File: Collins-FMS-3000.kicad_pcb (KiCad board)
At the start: 2 copper layers, 145 x 160 mm, 196 parts, among them J1 USB_B_Mini, J2 AVR-ISP-6, J3 Conn_01x04, SW1 SW_Push_LED, SW10 SW_Push_LED, SW11 SW_Push_LED, SW12 SW_Push_LED, SW13 SW_Push_LED, SW14 SW_Push_LED, SW15 SW_Push_LED, SW16 SW_Push_LED, SW17 SW_Push_LED, SW18 SW_Push_LED, SW19 SW_Push_LED, SW2 SW_Push_LED, SW20 SW_Push_LED, SW21 SW_Push_LED, SW22 SW_Push_LED, SW23 SW_Push_LED, SW24 SW_Push_LED, SW25 SW_Push_LED, SW26 SW_Push_LED, SW27 SW_Push_LED, SW28 SW_Push_LED, SW29 SW_Push_LED, SW3 SW_Push_LED, SW30 SW_Push_LED, SW31 SW_Push_LED, SW32 SW_Push_LED, SW33 SW_Push_LED, SW34 SW_Push_LED, SW35 SW_Push_LED, SW36 SW_Push_LED, SW37 SW_Push_LED, SW38 SW_Push_LED, SW39 SW_Push_LED, SW4 SW_Push_LED, SW40 SW_Push_LED, SW41 SW_Push_LED, SW42 SW_Push_LED, SW43 SW_Push_LED, SW44 SW_Push_LED, SW45 SW_Push_LED, SW46 SW_Push_LED, SW47 SW_Push_LED, SW48 SW_Push_LED, SW49 SW_Push_LED, SW5 SW_Push_LED, SW50 SW_Push_LED, SW51 SW_Push_LED, SW52 SW_Push_LED, SW53 SW_Push_LED, SW54 SW_Push_LED, SW55 SW_Push_LED, SW56 SW_Push_LED, SW57 SW_Push_LED, SW58 SW_Push_LED, SW59 SW_Push_LED, SW6 SW_Push_LED, SW60 SW_Push_LED, SW61 SW_Push_LED, SW62 SW_Push_LED, SW63 SW_Push_LED, SW64 SW_Push_LED, SW65 SW_Push_LED, SW66 SW_Push_LED, SW67 SW_Push_LED, SW68 SW_Push_LED, SW69 SW_Push_LED, SW7 SW_Push_LED, SW70 SW_Push, SW8 SW_Push_LED, SW9 SW_Push_LED, U1 ATmega32U4-MU, U2 MCP23017_SO, U3 MCP23017_SO, U4 IS31FL3733B, Y1 16MHz

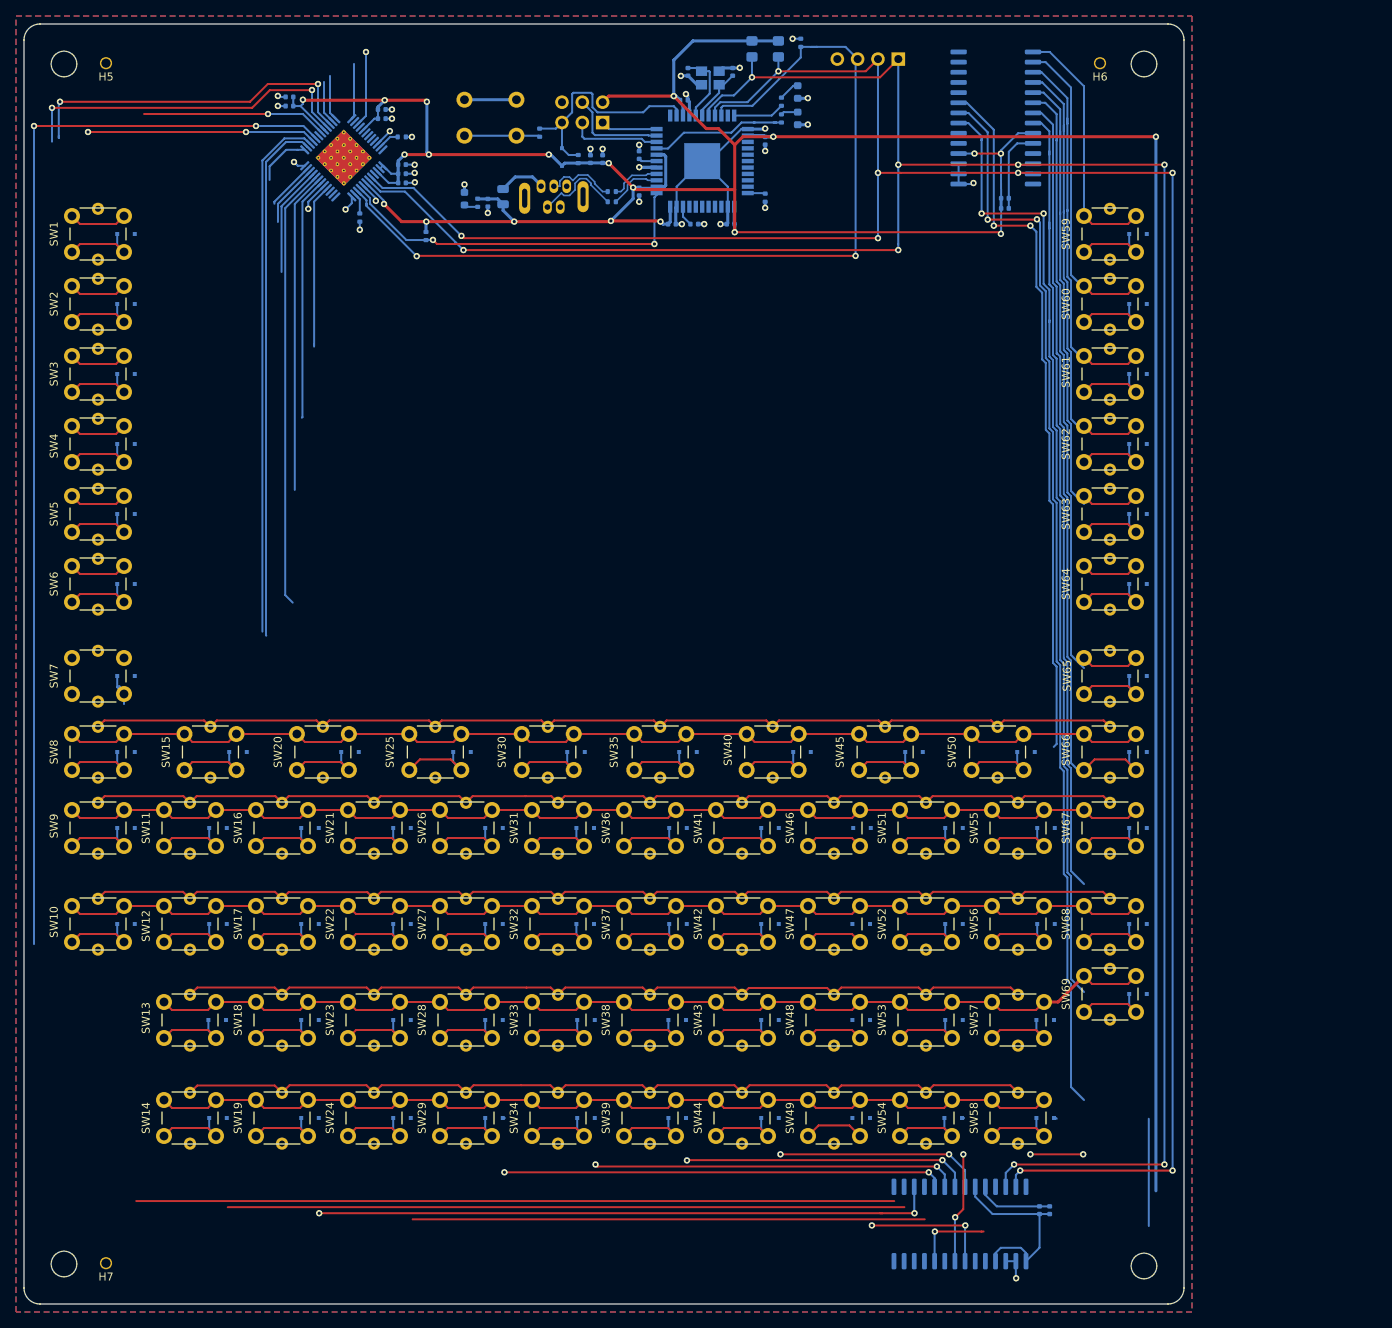
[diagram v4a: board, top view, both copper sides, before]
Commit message: Remove diodes, update interrupt connections
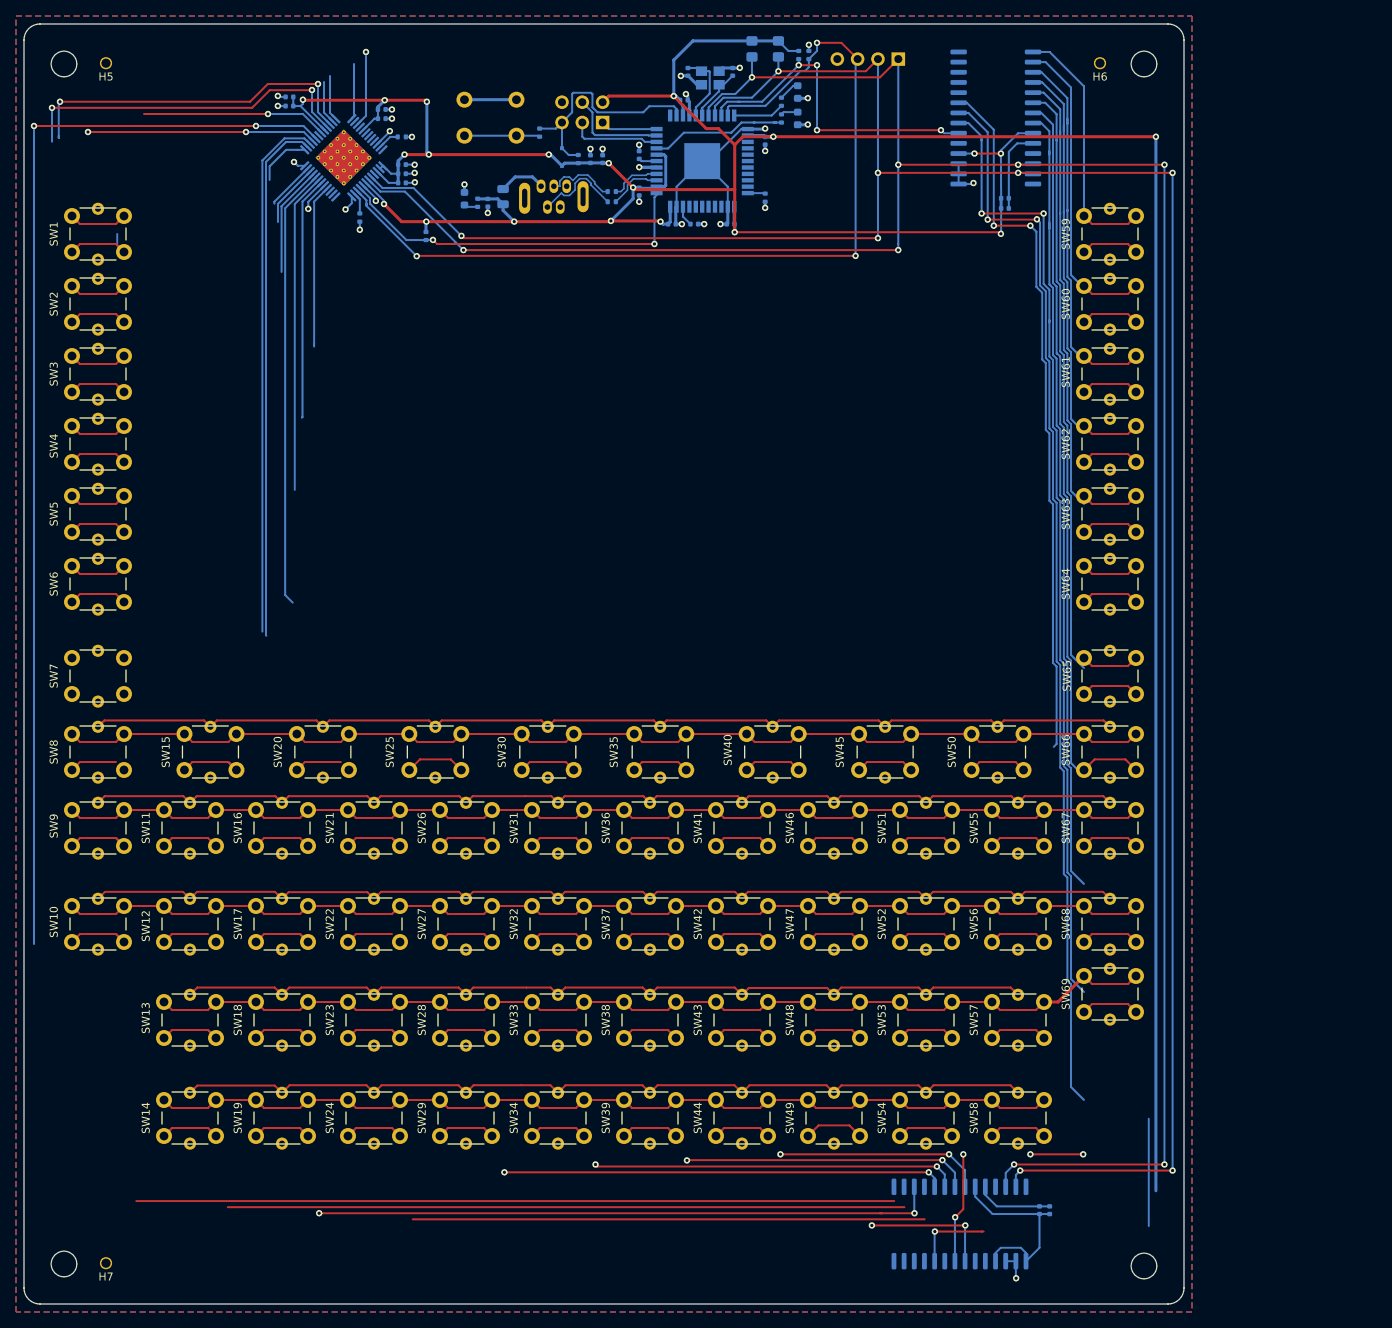
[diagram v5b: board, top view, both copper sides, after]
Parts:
- removed D1, D10, D11, D12, D13, D14, D15, D16, D17, D18, D19, D2, D20, D21, D22, D23, D24, D25, D26, D27, D28, D29, D3, D30, D31, D32, D33, D34, D35, D36, D37, D38, D39, D4, D40, D41, D42, D43, D44, D45, D46, D47, D48, D49, D5, D50, D51, D52, D53, D54, D55, D56, D57, D58, D59, D6, D60, D61, D62, D63, D64, D65, D66, D67, D68, D69, D7, D8, D9: D_Small, Diode_SMD:D_SOD-323F
- added R5: 100k, Resistor_SMD:R_0402_1005Metric, B.Cu at (116.8, 23.9)
- moved R3 1.83 mm to (118.1, 23.9)
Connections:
- net INTB renamed LED_INTB
- SW1 pad 2: Net-(D1-Pad2) -> /ButtonMatrix/COL0
- SW10 pad 2: Net-(D10-Pad2) -> /ButtonMatrix/COL0
- SW11 pad 2: Net-(D11-Pad2) -> /ButtonMatrix/COL1
- SW12 pad 2: Net-(D12-Pad2) -> /ButtonMatrix/COL1
- SW13 pad 2: Net-(D13-Pad2) -> /ButtonMatrix/COL1
- SW14 pad 2: Net-(D14-Pad2) -> /ButtonMatrix/COL1
- SW15 pad 2: Net-(D15-Pad2) -> /ButtonMatrix/COL2
- SW16 pad 2: Net-(D16-Pad2) -> /ButtonMatrix/COL2
- SW17 pad 2: Net-(D17-Pad2) -> /ButtonMatrix/COL2
- SW18 pad 2: Net-(D18-Pad2) -> /ButtonMatrix/COL2
- SW19 pad 2: Net-(D19-Pad2) -> /ButtonMatrix/COL2
- SW2 pad 2: Net-(D2-Pad2) -> /ButtonMatrix/COL0
- SW20 pad 2: Net-(D20-Pad2) -> /ButtonMatrix/COL3
- SW21 pad 2: Net-(D21-Pad2) -> /ButtonMatrix/COL3
- SW22 pad 2: Net-(D22-Pad2) -> /ButtonMatrix/COL3
- SW23 pad 2: Net-(D23-Pad2) -> /ButtonMatrix/COL3
- SW24 pad 2: Net-(D24-Pad2) -> /ButtonMatrix/COL3
- SW25 pad 2: Net-(D25-Pad2) -> /ButtonMatrix/COL4
- SW26 pad 2: Net-(D26-Pad2) -> /ButtonMatrix/COL4
- SW27 pad 2: Net-(D27-Pad2) -> /ButtonMatrix/COL4
- SW28 pad 2: Net-(D28-Pad2) -> /ButtonMatrix/COL4
- SW29 pad 2: Net-(D29-Pad2) -> /ButtonMatrix/COL4
- SW3 pad 2: Net-(D3-Pad2) -> /ButtonMatrix/COL0
- SW30 pad 2: Net-(D30-Pad2) -> /ButtonMatrix/COL5
- SW31 pad 2: Net-(D31-Pad2) -> /ButtonMatrix/COL5
- SW32 pad 2: Net-(D32-Pad2) -> /ButtonMatrix/COL5
- SW33 pad 2: Net-(D33-Pad2) -> /ButtonMatrix/COL5
- SW34 pad 2: Net-(D34-Pad2) -> /ButtonMatrix/COL5
- SW35 pad 2: Net-(D35-Pad2) -> /ButtonMatrix/COL6
- SW36 pad 2: Net-(D36-Pad2) -> /ButtonMatrix/COL6
- SW37 pad 2: Net-(D37-Pad2) -> /ButtonMatrix/COL6
- SW38 pad 2: Net-(D38-Pad2) -> /ButtonMatrix/COL6
- SW39 pad 2: Net-(D39-Pad2) -> /ButtonMatrix/COL6
- SW4 pad 2: Net-(D4-Pad2) -> /ButtonMatrix/COL0
- SW40 pad 2: Net-(D40-Pad2) -> /ButtonMatrix/COL7
- SW41 pad 2: Net-(D41-Pad2) -> /ButtonMatrix/COL7
- SW42 pad 2: Net-(D42-Pad2) -> /ButtonMatrix/COL7
- SW43 pad 2: Net-(D43-Pad2) -> /ButtonMatrix/COL7
- SW44 pad 2: Net-(D44-Pad2) -> /ButtonMatrix/COL7
- SW45 pad 2: Net-(D45-Pad2) -> /ButtonMatrix/COL8
- SW46 pad 2: Net-(D46-Pad2) -> /ButtonMatrix/COL8
- SW47 pad 2: Net-(D47-Pad2) -> /ButtonMatrix/COL8
- SW48 pad 2: Net-(D48-Pad2) -> /ButtonMatrix/COL8
- SW49 pad 2: Net-(D49-Pad2) -> /ButtonMatrix/COL8
- SW5 pad 2: Net-(D5-Pad2) -> /ButtonMatrix/COL0
- SW50 pad 2: Net-(D50-Pad2) -> /ButtonMatrix/COL9
- SW51 pad 2: Net-(D51-Pad2) -> /ButtonMatrix/COL9
- SW52 pad 2: Net-(D52-Pad2) -> /ButtonMatrix/COL9
- SW53 pad 2: Net-(D53-Pad2) -> /ButtonMatrix/COL9
- SW54 pad 2: Net-(D54-Pad2) -> /ButtonMatrix/COL9
- SW55 pad 2: Net-(D55-Pad2) -> /ButtonMatrix/COL10
- SW56 pad 2: Net-(D56-Pad2) -> /ButtonMatrix/COL10
- SW57 pad 2: Net-(D57-Pad2) -> /ButtonMatrix/COL10
- SW58 pad 2: Net-(D58-Pad2) -> /ButtonMatrix/COL10
- SW59 pad 2: Net-(D59-Pad2) -> /ButtonMatrix/COL11
- SW6 pad 2: Net-(D6-Pad2) -> /ButtonMatrix/COL0
- SW60 pad 2: Net-(D60-Pad2) -> /ButtonMatrix/COL11
- SW61 pad 2: Net-(D61-Pad2) -> /ButtonMatrix/COL11
- SW62 pad 2: Net-(D62-Pad2) -> /ButtonMatrix/COL11
- SW63 pad 2: Net-(D63-Pad2) -> /ButtonMatrix/COL11
- SW64 pad 2: Net-(D64-Pad2) -> /ButtonMatrix/COL11
- SW65 pad 2: Net-(D65-Pad2) -> /ButtonMatrix/COL11
- SW66 pad 2: Net-(D66-Pad2) -> /ButtonMatrix/COL11
- SW67 pad 2: Net-(D67-Pad2) -> /ButtonMatrix/COL11
- SW68 pad 2: Net-(D68-Pad2) -> /ButtonMatrix/COL11
- SW69 pad 2: Net-(D69-Pad2) -> /ButtonMatrix/COL11
- SW7 pad 2: Net-(D7-Pad2) -> /ButtonMatrix/COL0
- SW8 pad 2: Net-(D8-Pad2) -> /ButtonMatrix/COL0
- SW9 pad 2: Net-(D9-Pad2) -> /ButtonMatrix/COL0
- U1 pad 20: SDB -> ROW_INTA
- U1 pad 21: Net-(U1-Pad21) -> SDB
- U2 pad 20: Net-(U2-Pad20) -> ROW_INTA
- U4 pad 43: +5V -> GND
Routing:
- net /ButtonMatrix/COL11: track 23.2 -> 97.5 mm
- net /ButtonMatrix/COL0: track 94.7 -> 164.6 mm
- net ROW_INTA: track 0.00 -> 42.1 mm, vias 0 -> 4
- net /ButtonMatrix/COL2: track 78.3 -> 118.6 mm
- net /ButtonMatrix/COL4: track 55.4 -> 94.6 mm
- net /ButtonMatrix/COL8: track 16.2 -> 53.1 mm
- net /ButtonMatrix/COL5: track 45.9 -> 82.6 mm
- net /ButtonMatrix/COL7: track 26.0 -> 62.7 mm
- net /ButtonMatrix/COL6: track 36.1 -> 72.8 mm
- net /ButtonMatrix/COL9: track 13.9 -> 50.4 mm
- net /ButtonMatrix/COL3: track 64.0 -> 100.2 mm
- net /ButtonMatrix/COL1: track 84.6 -> 113.8 mm
- net /ButtonMatrix/COL10: track 0.14 -> 29.3 mm
- net Net-(D69-Pad2): track 10.9 -> 0.00 mm
- net Net-(D25-Pad2): track 10.3 -> 0.00 mm
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
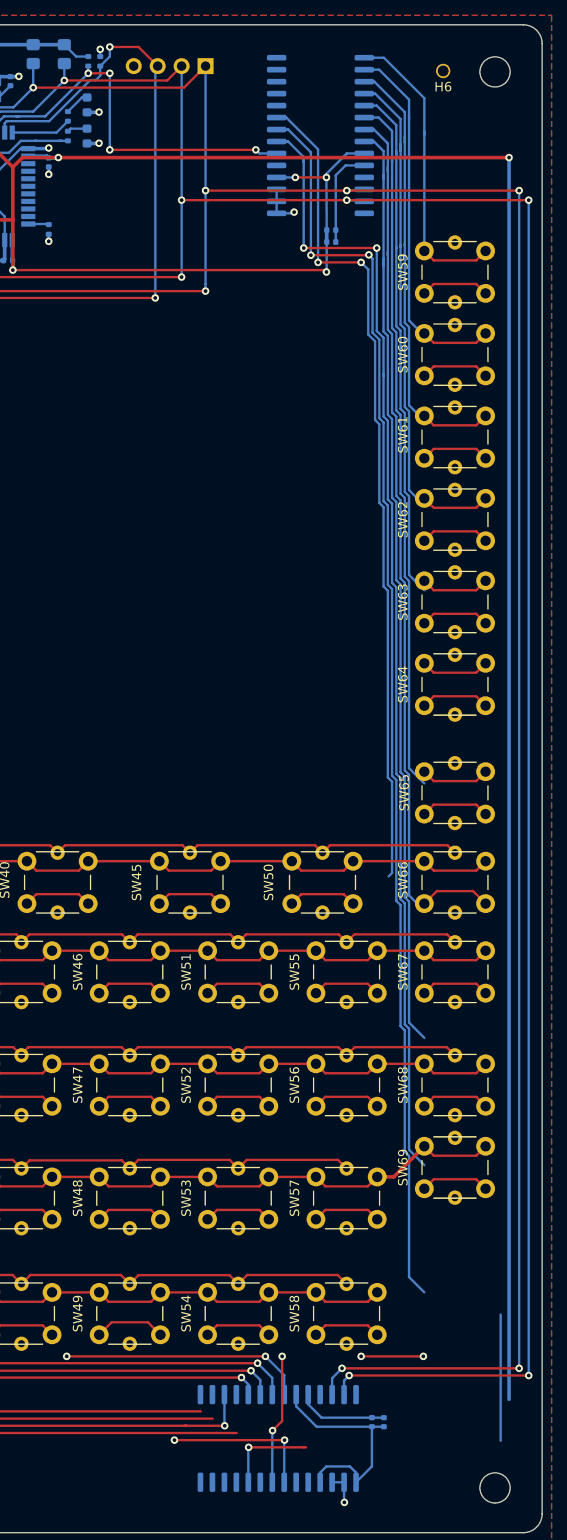
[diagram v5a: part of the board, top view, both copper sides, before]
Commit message: Connect unused pins
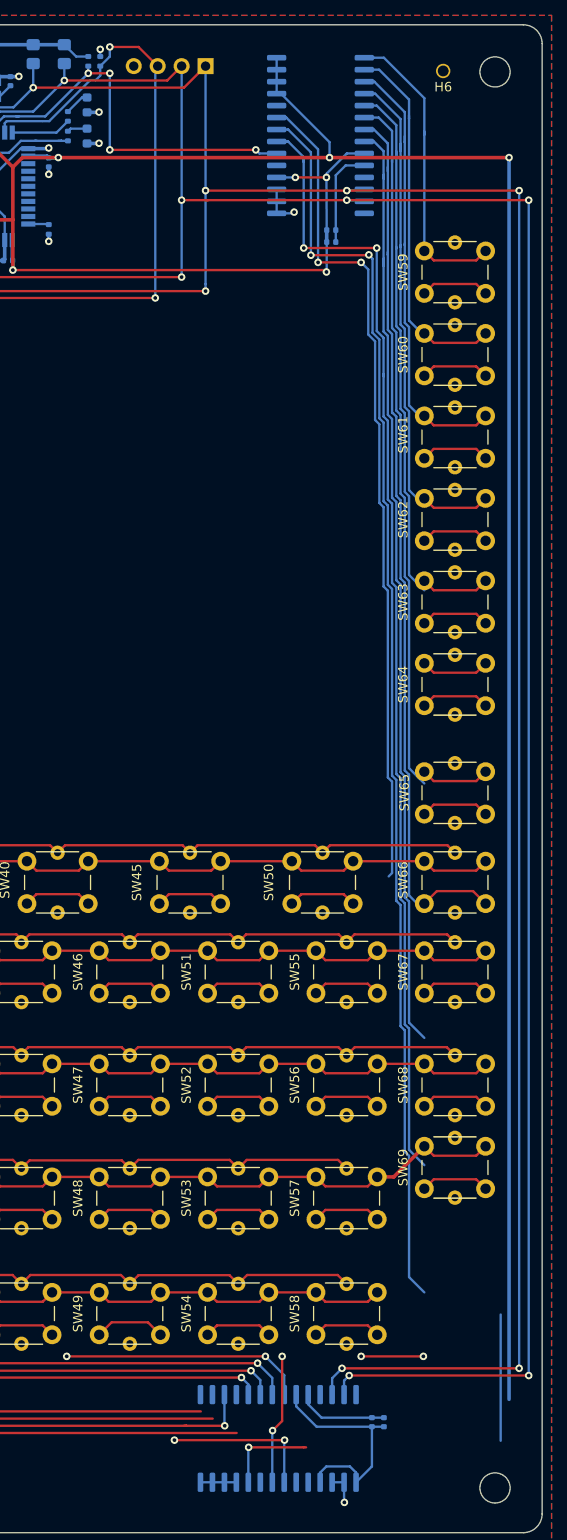
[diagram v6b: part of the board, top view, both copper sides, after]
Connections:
- U2 pad 25: Net-(U2-Pad25) -> +5V
- U2 pad 26: Net-(U2-Pad26) -> +5V
- U2 pad 27: Net-(U2-Pad27) -> +5V
- U2 pad 28: Net-(U2-Pad28) -> +5V
- U3 pad 25: Net-(U3-Pad25) -> +5V
- U3 pad 26: Net-(U3-Pad26) -> +5V
- U3 pad 27: Net-(U3-Pad27) -> +5V
- U3 pad 28: Net-(U3-Pad28) -> +5V
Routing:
- net +5V: track 482.7 -> 499.7 mm, vias 20 -> 21
